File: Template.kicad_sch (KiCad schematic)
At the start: 22 parts, among them J1 OLED, SW1 SW_Push, U1 ProMicro

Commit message: Reset to blank
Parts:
- removed D1, D2, D3, D4, D5, D6, D7, D8, D9: D_Small, bevin:D3_TH_nonHybrid, symbol Device:D_Small
- removed J1: OLED, bevin:OLED_v2, symbol Connector_Generic:Conn_01x04
- removed MX1, MX2, MX3, MX4, MX5, MX6, MX7, MX8, MX9: MX-NoLED, bevin:MXOnly-1U-NoLED, symbol mx:MX-NoLED
- removed R1: 10k, bevin:R3_TH_nonHybrid, symbol Device:R
- removed SW1: SW_Push, Button_Switch_SMD:SW_SPST_TL3342, symbol Switch:SW_Push
- removed U1: ProMicro, bevin:ProMicro_v3, symbol promicro:ProMicro
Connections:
- no-connect marks 8 -> 0

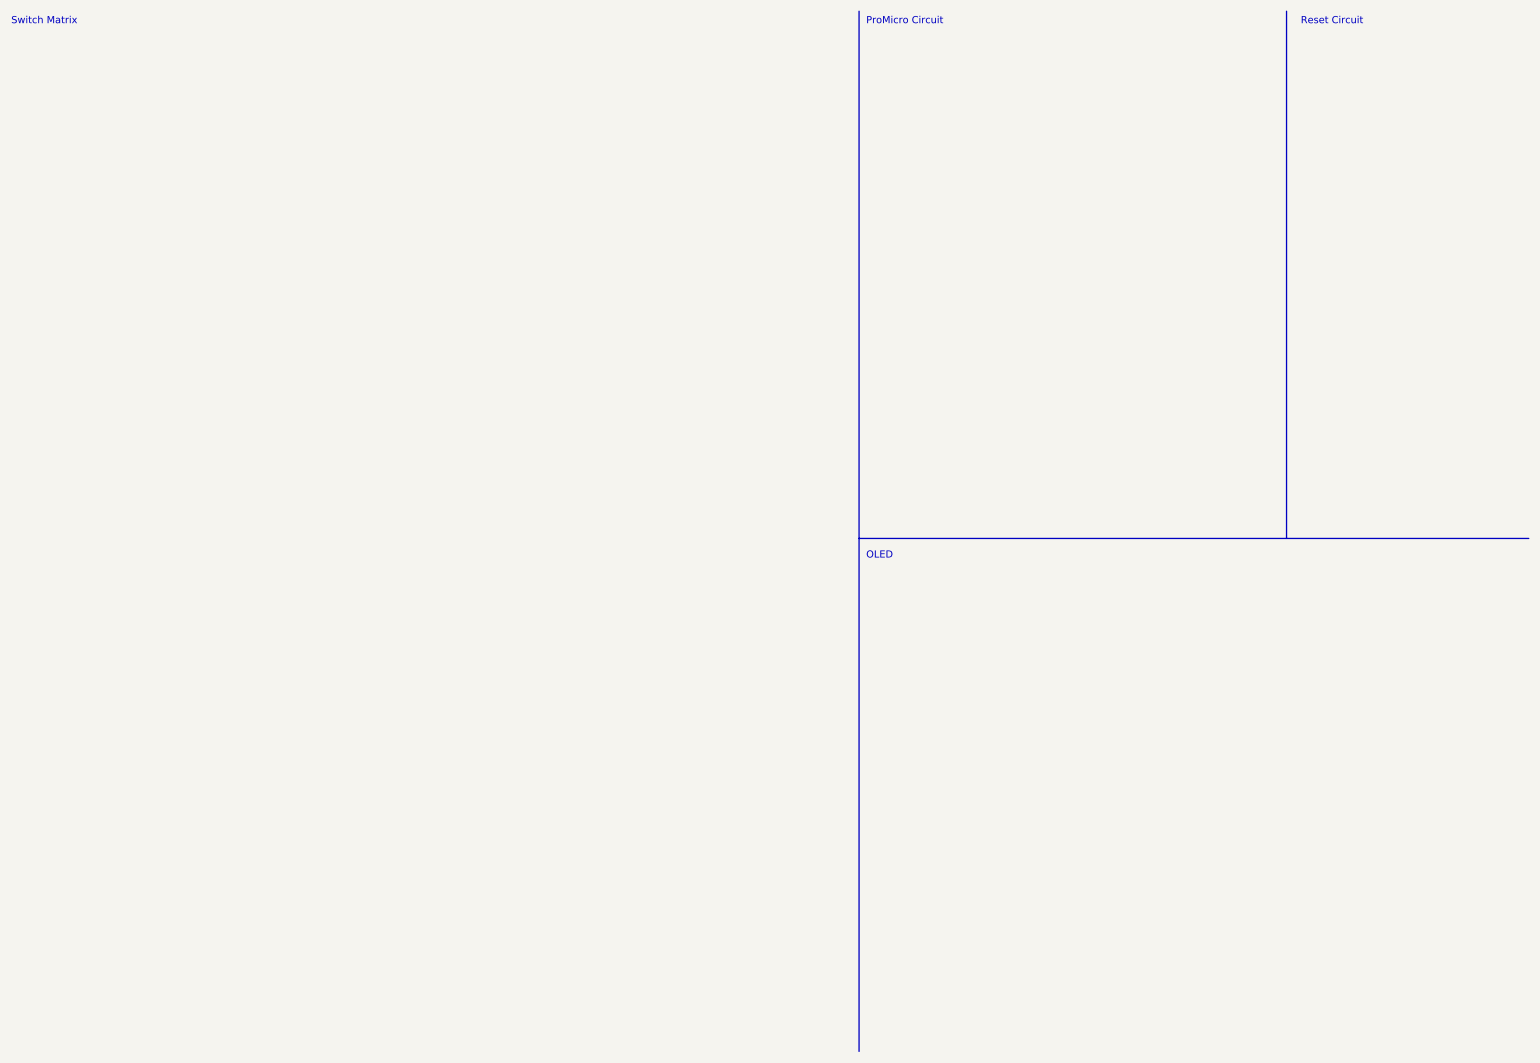
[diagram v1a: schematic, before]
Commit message: Added symbol to table
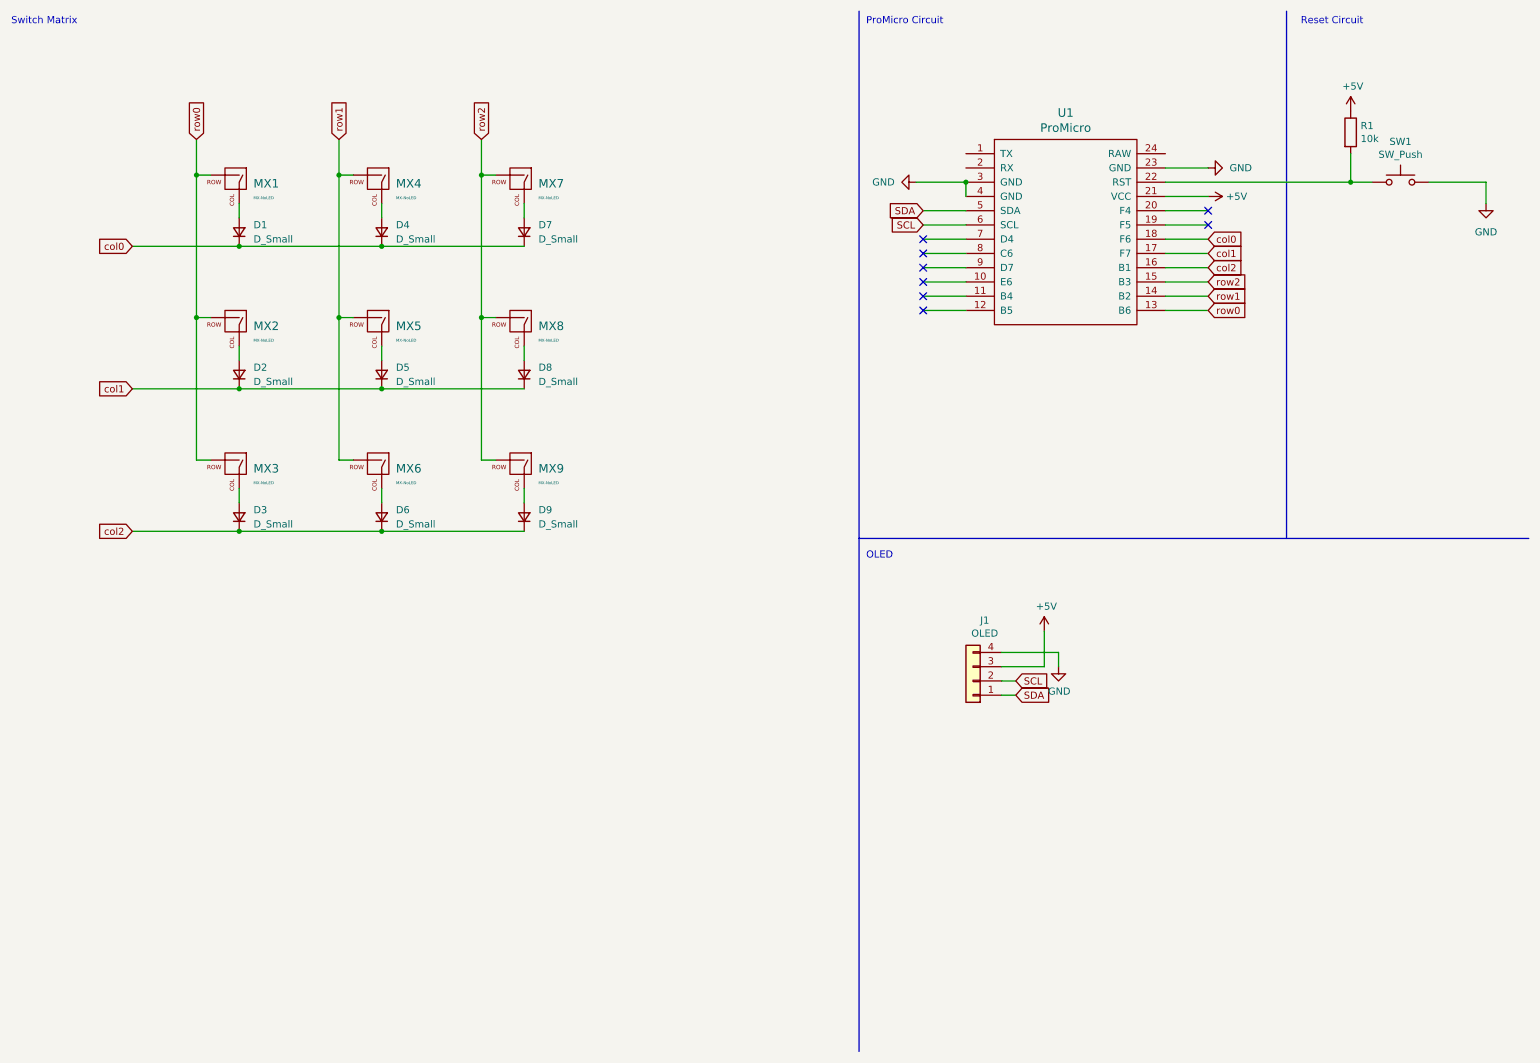
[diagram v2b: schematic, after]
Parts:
- added D1, D2, D3, D4, D5, D6, D7, D8, D9: D_Small, bevin:D3_TH_nonHybrid, symbol Device:D_Small
- added J1: OLED, bevin:OLED_v2, symbol Connector_Generic:Conn_01x04
- added MX1, MX2, MX3, MX4, MX5, MX6, MX7, MX8, MX9: MX-NoLED, bevin:MXOnly-1U-NoLED, symbol mx:MX-NoLED
- added R1: 10k, bevin:R3_TH_nonHybrid, symbol Device:R
- added SW1: SW_Push, Button_Switch_SMD:SW_SPST_TL3342, symbol Switch:SW_Push
- added U1: ProMicro, bevin:ProMicro_v3, symbol promicro:ProMicro
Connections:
- new net: D2.2 (A), MX2.1 (COL)
- new net: D7.2 (A), MX7.1 (COL)
- new net: R1.2, SW1.1, U1.22 (RST)
- new net: D5.2 (A), MX5.1 (COL)
- new net: D4.2 (A), MX4.1 (COL)
- new net: D9.2 (A), MX9.1 (COL)
- new net: D1.2 (A), MX1.1 (COL)
- new net: D8.2 (A), MX8.1 (COL)
- new net: D6.2 (A), MX6.1 (COL)
- new net: D3.2 (A), MX3.1 (COL)
- new net +5V: J1.3 (Pin_3), R1.1, U1.21 (VCC)
- new net GND: J1.4 (Pin_4), SW1.2, U1.23 (GND), U1.3 (GND), U1.4 (GND)
- new net SCL: J1.2 (Pin_2), U1.6 (SCL)
- new net SDA: J1.1 (Pin_1), U1.5 (SDA)
- new net col0: D1.1 (K), D4.1 (K), D7.1 (K), U1.18 (F6)
- new net col1: D2.1 (K), D5.1 (K), D8.1 (K), U1.17 (F7)
- new net col2: D3.1 (K), D6.1 (K), D9.1 (K), U1.16 (B1)
- new net row0: MX1.2 (ROW), MX2.2 (ROW), MX3.2 (ROW), U1.13 (B6)
- new net row1: MX4.2 (ROW), MX5.2 (ROW), MX6.2 (ROW), U1.14 (B2)
- new net row2: MX7.2 (ROW), MX8.2 (ROW), MX9.2 (ROW), U1.15 (B3)
- no-connect marks 0 -> 8
